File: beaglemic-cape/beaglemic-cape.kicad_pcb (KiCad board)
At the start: 2 copper layers, 79 parts, among them J1 USB_OTG, J10 MIC-04, J11 MIC-06, J12 MIC-08, J13 MIC-10, J14 MIC-12, J15 MIC-14, J16 MIC-01, J17 MIC-03, J18 MIC-05, J19 MIC-07, J2 PB_P1, J20 MIC-09, J21 MIC-11, J22 MIC-13, J23 MIC-15, J24 BBAI_FAN, J3 EXT_5V, J4 PB_P2, J5 BBAI_P8, J6 ICE40_EXT, J7 BBAI_P9, J8 MIC-00, J9 MIC-02, U1 74HC595, U2 74HC595, U3 AMS1117, U4 74HCT244, U5 SPM0423HD4H-WB, U6 SPM0423HD4H-WB

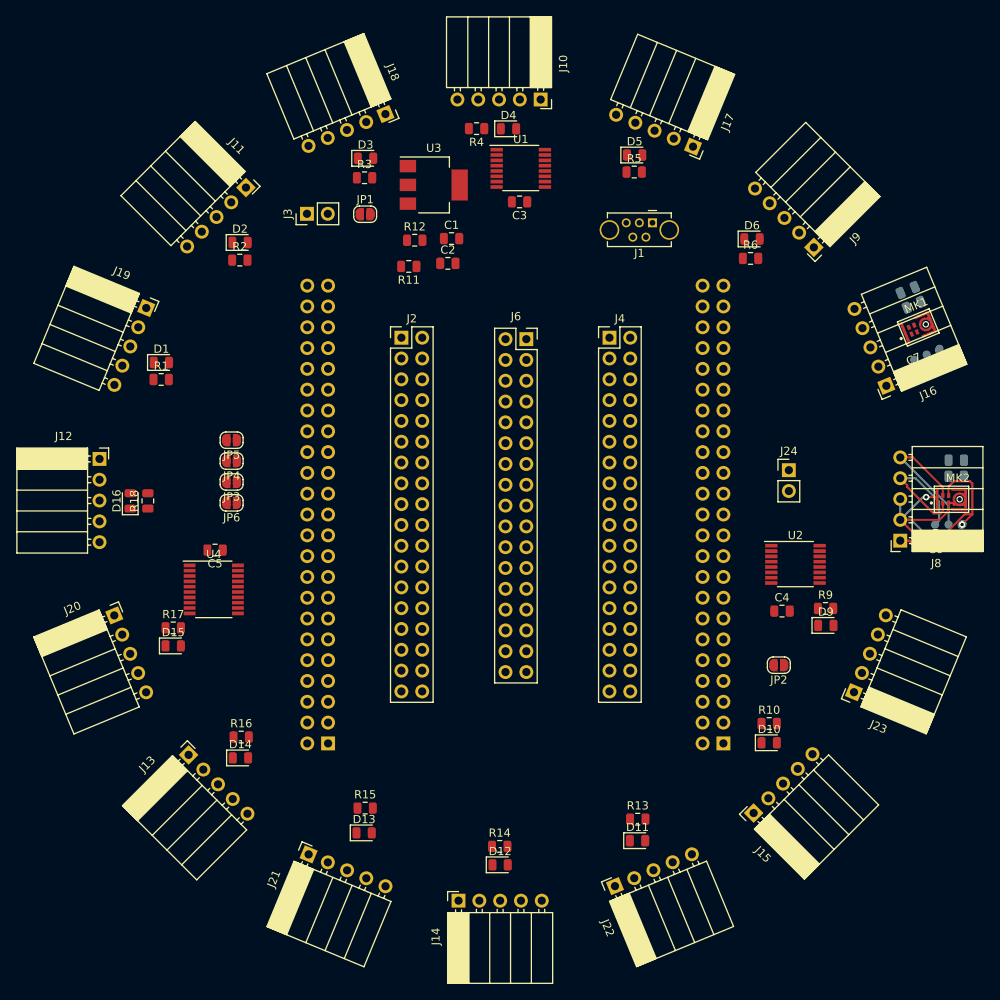
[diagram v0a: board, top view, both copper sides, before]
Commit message: beaglemic-cape: Shrink PCB to 100x100mm
Let's keep the PCB in the hobby price range.

Version 1.0-rc2

TODO: Route me!

Signed-off-by: Dimitar Dimitrov <dimitar@dinux.eu>
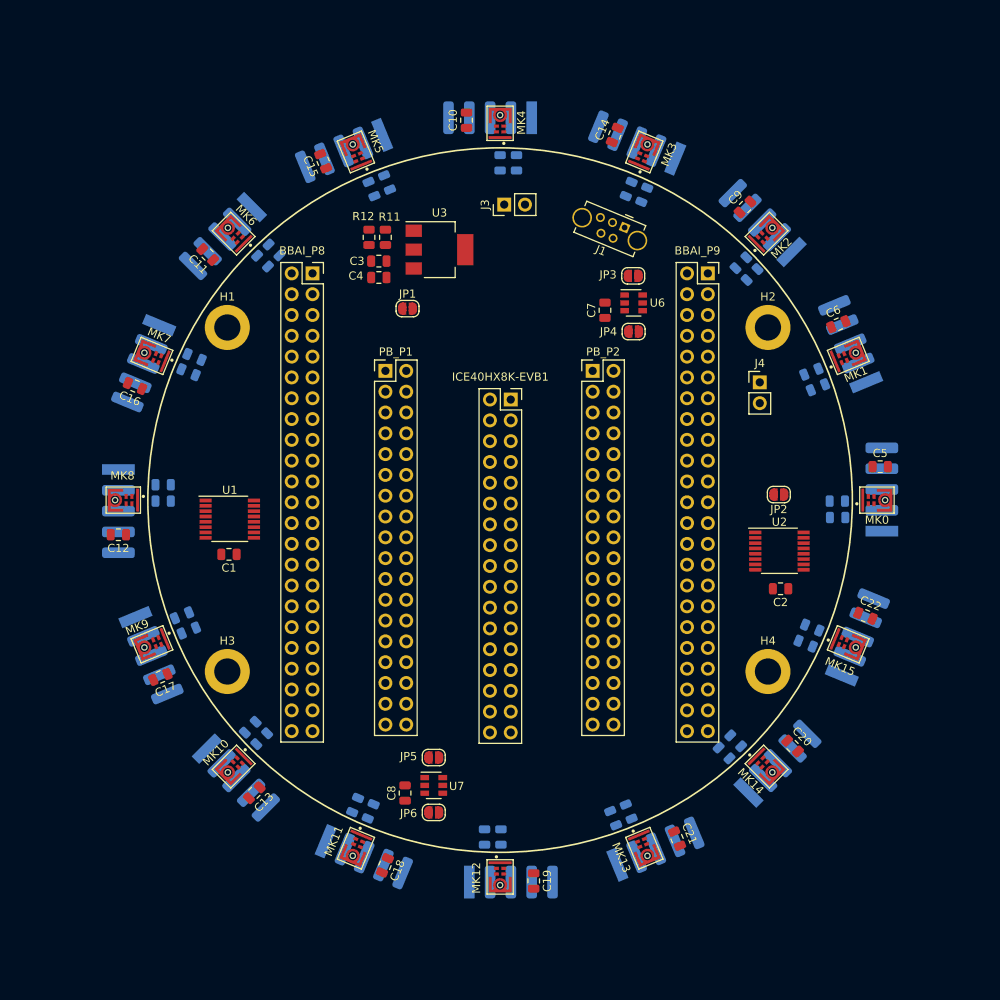
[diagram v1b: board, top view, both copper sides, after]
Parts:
- removed D16: LED-08, LED_SMD:LED_0805_2012Metric
- removed J10: MIC-04, Connector_PinSocket_2.54mm:PinSocket_1x05_P2.54mm_Horizontal
- removed J11: MIC-06, Connector_PinSocket_2.54mm:PinSocket_1x05_P2.54mm_Horizontal
- removed J12: MIC-08, Connector_PinSocket_2.54mm:PinSocket_1x05_P2.54mm_Horizontal
- removed J13: MIC-10, Connector_PinSocket_2.54mm:PinSocket_1x05_P2.54mm_Horizontal
- removed J14: MIC-12, Connector_PinSocket_2.54mm:PinSocket_1x05_P2.54mm_Horizontal
- removed J15: MIC-14, Connector_PinSocket_2.54mm:PinSocket_1x05_P2.54mm_Horizontal
- removed J16: MIC-01, Connector_PinSocket_2.54mm:PinSocket_1x05_P2.54mm_Horizontal
- removed J17: MIC-03, Connector_PinSocket_2.54mm:PinSocket_1x05_P2.54mm_Horizontal
- removed J18: MIC-05, Connector_PinSocket_2.54mm:PinSocket_1x05_P2.54mm_Horizontal
- removed J19: MIC-07, Connector_PinSocket_2.54mm:PinSocket_1x05_P2.54mm_Horizontal
- removed J2: PB_P1, Connector_PinHeader_2.54mm:PinHeader_2x18_P2.54mm_Vertical
- removed J20: MIC-09, Connector_PinSocket_2.54mm:PinSocket_1x05_P2.54mm_Horizontal
- removed J21: MIC-11, Connector_PinSocket_2.54mm:PinSocket_1x05_P2.54mm_Horizontal
- removed J22: MIC-13, Connector_PinSocket_2.54mm:PinSocket_1x05_P2.54mm_Horizontal
- removed J23: MIC-15, Connector_PinSocket_2.54mm:PinSocket_1x05_P2.54mm_Horizontal
- removed J24: BBAI_FAN, Connector_PinHeader_2.54mm:PinHeader_1x02_P2.54mm_Vertical
- removed J5: BBAI_P8, Connector_PinSocket_2.54mm:PinSocket_2x23_P2.54mm_Vertical
- removed J6: ICE40_EXT, Connector_PinSocket_2.54mm:PinSocket_2x17_P2.54mm_Vertical
- removed J7: BBAI_P9, Connector_PinSocket_2.54mm:PinSocket_2x23_P2.54mm_Vertical
- removed J8: MIC-00, Connector_PinSocket_2.54mm:PinSocket_1x05_P2.54mm_Horizontal
- removed J9: MIC-02, Connector_PinSocket_2.54mm:PinSocket_1x05_P2.54mm_Horizontal
- removed U4: 74HCT244, Package_SO:TSSOP-20_4.4x6.5mm_P0.65mm
- removed U5: SPM0423HD4H-WB, bga-6:BGA_6
- added BBAI_P8: BBAI_P8, Connector_PinSocket_2.54mm:PinSocket_2x23_P2.54mm_Vertical, F.Cu at (110.4, 66.4)
- added BBAI_P9: BBAI_P9, Connector_PinSocket_2.54mm:PinSocket_2x23_P2.54mm_Vertical, F.Cu at (158.7, 66.4)
- added C10: 100n, Capacitor_SMD:C_0805_2012Metric, F.Cu at (129.2, 47.7)
- added C11: 100n, Capacitor_SMD:C_0805_2012Metric, F.Cu at (97.6, 64.1)
- added C12: 100n, Capacitor_SMD:C_0805_2012Metric, F.Cu at (86.7, 98.3)
- added C13: 100n, Capacitor_SMD:C_0805_2012Metric, F.Cu at (103.3, 129.8)
- added C14: 100n, Capacitor_SMD:C_0805_2012Metric, F.Cu at (147.3, 49.5)
- added C15: 100n, Capacitor_SMD:C_0805_2012Metric, F.Cu at (111.7, 52.7)
- added C16: 100n, Capacitor_SMD:C_0805_2012Metric, F.Cu at (88.7, 80.1)
- added C17: 100n, Capacitor_SMD:C_0805_2012Metric, F.Cu at (91.8, 115.7)
- added C18: 100n, Capacitor_SMD:C_0805_2012Metric, F.Cu at (119.2, 138.7)
- added C19: 100n, Capacitor_SMD:C_0805_2012Metric, F.Cu at (137.4, 140.6)
- added C20: 100n, Capacitor_SMD:C_0805_2012Metric, F.Cu at (169.0, 124.1)
- added C21: 100n, Capacitor_SMD:C_0805_2012Metric, F.Cu at (154.9, 135.4)
- added C22: 100n, Capacitor_SMD:C_0805_2012Metric, F.Cu at (177.9, 108.2)
- added C8: 100n, Capacitor_SMD:C_0805_2012Metric, F.Cu at (121.7, 129.8)
- added C9: 100n, Capacitor_SMD:C_0805_2012Metric, F.Cu at (163.2, 58.3)
- added D0: LED-00, LED_SMD:LED_0805_2012Metric, B.Cu at (174.5, 94.2)
- added H1: MountingHole_Pad, MountingHole:MountingHole_3.2mm_M3_ISO14580_Pad, F.Cu at (100.0, 73.0)
- added H2: MountingHole_Pad, MountingHole:MountingHole_3.2mm_M3_ISO14580_Pad, F.Cu at (166.0, 73.0)
- added H3: MountingHole_Pad, MountingHole:MountingHole_3.2mm_M3_ISO14580_Pad, F.Cu at (100.0, 115.0)
- added H4: MountingHole_Pad, MountingHole:MountingHole_3.2mm_M3_ISO14580_Pad, F.Cu at (166.0, 115.0)
- added ICE40HX8K-EVB1: ICE40_EXT, Connector_PinSocket_2.54mm:PinSocket_2x17_P2.54mm_Vertical, F.Cu at (134.6, 81.8)
- added MK0: INMP621, inmp621-footprint:MK_INMP621, F.Cu at (179.3, 94.1)
- added MK10: INMP621, inmp621-footprint:MK_INMP621, F.Cu at (100.8, 126.6)
- added MK11: INMP621, inmp621-footprint:MK_INMP621, F.Cu at (115.7, 136.6)
- added MK12: INMP621, inmp621-footprint:MK_INMP621, F.Cu at (133.3, 140.1)
- added MK13: INMP621, inmp621-footprint:MK_INMP621, F.Cu at (150.9, 136.6)
- added MK14: INMP621, inmp621-footprint:MK_INMP621, F.Cu at (165.8, 126.6)
- added MK15: INMP621, inmp621-footprint:MK_INMP621, F.Cu at (175.8, 111.7)
- added MK3: INMP621, inmp621-footprint:MK_INMP621, F.Cu at (150.9, 51.6)
- added MK4: INMP621, inmp621-footprint:MK_INMP621, F.Cu at (133.3, 48.1)
- added MK5: INMP621, inmp621-footprint:MK_INMP621, F.Cu at (115.7, 51.6)
- added MK6: INMP621, inmp621-footprint:MK_INMP621, F.Cu at (100.8, 61.5)
- added MK7: INMP621, inmp621-footprint:MK_INMP621, F.Cu at (90.8, 76.5)
- added MK8: INMP621, inmp621-footprint:MK_INMP621, F.Cu at (87.3, 94.1)
- added MK9: INMP621, inmp621-footprint:MK_INMP621, F.Cu at (90.8, 111.7)
- added PB_P1: PB_P1, Connector_PinHeader_2.54mm:PinHeader_2x18_P2.54mm_Vertical, F.Cu at (119.3, 78.3)
- added PB_P2: PB_P2, Connector_PinHeader_2.54mm:PinHeader_2x18_P2.54mm_Vertical, F.Cu at (144.6, 78.3)
- added PHM-0: MIC-00, pinheader-smd:pinheader-5-smd-pads, B.Cu at (179.9, 87.7)
- added PHM-1: MIC-01, pinheader-smd:pinheader-5-smd-pads, B.Cu at (174.1, 70.3)
- added PHM-10: MIC-10, pinheader-smd:pinheader-5-smd-pads, B.Cu at (104.7, 131.6)
- added PHM-11: MIC-11, pinheader-smd:pinheader-5-smd-pads, B.Cu at (121.4, 139.6)
- added PHM-12: MIC-12, pinheader-smd:pinheader-5-smd-pads, B.Cu at (139.7, 140.7)
- added PHM-13: MIC-13, pinheader-smd:pinheader-5-smd-pads, B.Cu at (157.0, 134.7)
- added PHM-14: MIC-14, pinheader-smd:pinheader-5-smd-pads, B.Cu at (170.8, 122.6)
- added PHM-15: MIC-15, pinheader-smd:pinheader-5-smd-pads, B.Cu at (178.9, 106.1)
- added PHM-2: MIC-02, pinheader-smd:pinheader-5-smd-pads, B.Cu at (161.7, 56.6)
- added PHM-3: MIC-03, pinheader-smd:pinheader-5-smd-pads, B.Cu at (145.3, 48.5)
- added PHM-4: MIC-04, pinheader-smd:pinheader-5-smd-pads, B.Cu at (127.0, 47.4)
- added PHM-5: MIC-05, pinheader-smd:pinheader-5-smd-pads, B.Cu at (109.5, 53.4)
- added PHM-6: MIC-06, pinheader-smd:pinheader-5-smd-pads, B.Cu at (95.8, 65.5)
- added PHM-7: MIC-07, pinheader-smd:pinheader-5-smd-pads, B.Cu at (87.8, 82.1)
- added PHM-8: MIC-08, pinheader-smd:pinheader-5-smd-pads, B.Cu at (86.7, 100.5)
- added PHM-9: MIC-09, pinheader-smd:pinheader-5-smd-pads, B.Cu at (92.7, 117.7)
- added U7: 74AUC2G34, Package_TO_SOT_SMD:SOT-23-6, F.Cu at (125.2, 128.9)
- C2: value 10u -> 100n
- C4: value 100n -> 10u
- D1: value LED-07 -> LED-01; moved to B.Cu
- D10: value LED-14 -> LED-10; moved to B.Cu
- D11: value LED-13 -> LED-11; moved to B.Cu
- D12, D4, R1, R10, R13, R14, R15, R16, R17, R18, R2, R3, R4, R5, R6, R9: moved to B.Cu
- D13: value LED-11 -> LED-13; moved to B.Cu
- D14: value LED-10 -> LED-14; moved to B.Cu
- D15: value LED-09 -> LED-15; moved to B.Cu
- D2: value LED-06 -> LED-02; moved to B.Cu
- D3: value LED-05 -> LED-03; moved to B.Cu
- D5: value LED-03 -> LED-05; moved to B.Cu
- D6: value LED-02 -> LED-06; moved to B.Cu
- D7: value LED-01 -> LED-07
- D8: value LED-00 -> LED-08
- D9: value LED-15 -> LED-09; moved to B.Cu
- J4: value PB_P2 -> BBAI_FAN; footprint Connector_PinHeader_2.54mm:PinHeader_2x18_P2.54mm_Vertical -> Connector_PinHeader_2.54mm:PinHeader_1x02_P2.54mm_Vertical
- U6: value SPM0423HD4H-WB -> 74AUC2G34; footprint bga-6:BGA_6 -> Package_TO_SOT_SMD:SOT-23-6; moved to F.Cu
- moved D8 96.9 mm to (92.2, 94.2)
- moved D7 88.9 mm to (95.3, 78.5), turned to 337.5 degrees
- moved C5 81.8 mm to (179.7, 90.0), turned to 0 degrees
- moved D1 79.4 mm to (171.3, 78.4), turned to 202.5 degrees
- moved D15 78.0 mm to (171.4, 109.6), turned to 157.5 degrees
- moved D9 77.8 mm to (95.3, 110.0), turned to 22.5 degrees
- moved C4 63.9 mm to (118.5, 66.9), turned to 180 degrees
- moved D10 62.0 mm to (104.2, 123.2), turned to 45 degrees
- moved D2 61.2 mm to (162.7, 65.1), turned to 225 degrees
- moved D14 60.5 mm to (162.1, 123.5), turned to 135 degrees
- moved D6 59.8 mm to (104.3, 64.9), turned to 315 degrees
- moved C2 56.8 mm to (167.5, 104.9), turned to 180 degrees
- moved U1 55.6 mm to (100.3, 96.4)
- moved JP3 55.1 mm to (149.6, 66.7), turned to 0 degrees
- moved JP4 51.6 mm to (149.6, 73.5), turned to 0 degrees
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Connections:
- J4 pad 1: (no net) -> GND
- J4 pad 2: (no net) -> +5V
- MK2 pad 5: /MIC_D0 -> /MIC_D1
- R1 pad 1: Net-(D1-Pad1) -> Net-(D7-Pad1)
- R10 pad 1: Net-(D10-Pad1) -> Net-(D14-Pad1)
- R13 pad 1: Net-(D11-Pad1) -> Net-(D13-Pad1)
- R15 pad 1: Net-(D13-Pad1) -> Net-(D11-Pad1)
- R16 pad 1: Net-(D14-Pad1) -> Net-(D10-Pad1)
- R17 pad 1: Net-(D15-Pad1) -> Net-(D9-Pad1)
- R18 pad 1: Net-(D16-Pad1) -> Net-(D8-Pad1)
- R2 pad 1: Net-(D2-Pad1) -> Net-(D6-Pad1)
- R3 pad 1: Net-(D3-Pad1) -> Net-(D5-Pad1)
- R5 pad 1: Net-(D5-Pad1) -> Net-(D3-Pad1)
- R6 pad 1: Net-(D6-Pad1) -> Net-(D2-Pad1)
- R7 pad 1: Net-(D7-Pad1) -> Net-(D1-Pad1)
- R8 pad 1: Net-(D8-Pad1) -> Net-(D0-Pad1)
- R9 pad 1: Net-(D9-Pad1) -> Net-(D15-Pad1)
- U1 pad 1: Net-(D7-Pad2) -> Net-(D1-Pad2)
- U1 pad 15: Net-(D8-Pad2) -> Net-(D0-Pad2)
- U1 pad 2: Net-(D6-Pad2) -> Net-(D2-Pad2)
- U1 pad 3: Net-(D5-Pad2) -> Net-(D3-Pad2)
- U1 pad 5: Net-(D3-Pad2) -> Net-(D5-Pad2)
- U1 pad 6: Net-(D2-Pad2) -> Net-(D6-Pad2)
- U1 pad 7: Net-(D1-Pad2) -> Net-(D7-Pad2)
- U2 pad 1: Net-(D15-Pad2) -> Net-(D9-Pad2)
- U2 pad 15: Net-(D16-Pad2) -> Net-(D8-Pad2)
- U2 pad 2: Net-(D14-Pad2) -> Net-(D10-Pad2)
- U2 pad 3: Net-(D13-Pad2) -> Net-(D11-Pad2)
- U2 pad 5: Net-(D11-Pad2) -> Net-(D13-Pad2)
- U2 pad 6: Net-(D10-Pad2) -> Net-(D14-Pad2)
- U2 pad 7: Net-(D9-Pad2) -> Net-(D15-Pad2)
- U6 pad 1: GND -> /MIC_CLK
- U6 pad 2: +3V3 -> GND
- U6 pad 3: GND -> /MIC_CLK
- U6 pad 4: /Microphone Headers/CLK0 -> /Microphone Headers/CLK1
- U6 pad 5: /MIC_D0 -> +3V3
- U6 pad 6: +3V3 -> /Microphone Headers/CLK0
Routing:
- net GND: track 31.2 -> 0.00 mm, vias 1 -> 0
- net +3V3: track 20.4 -> 0.00 mm, vias 1 -> 0
- net /MIC_D0: track 18.4 -> 0.00 mm
- net /Microphone Headers/CLK0: track 17.2 -> 0.00 mm
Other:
- net class Power added: clearance 0.2, trace_width 0.4, via_dia 0.8, via_drill 0.4

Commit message: beaglemic-cape: Route PCB
WARNING - NOT TESTED YET!

Signed-off-by: Dimitar Dimitrov <dimitar@dinux.eu>
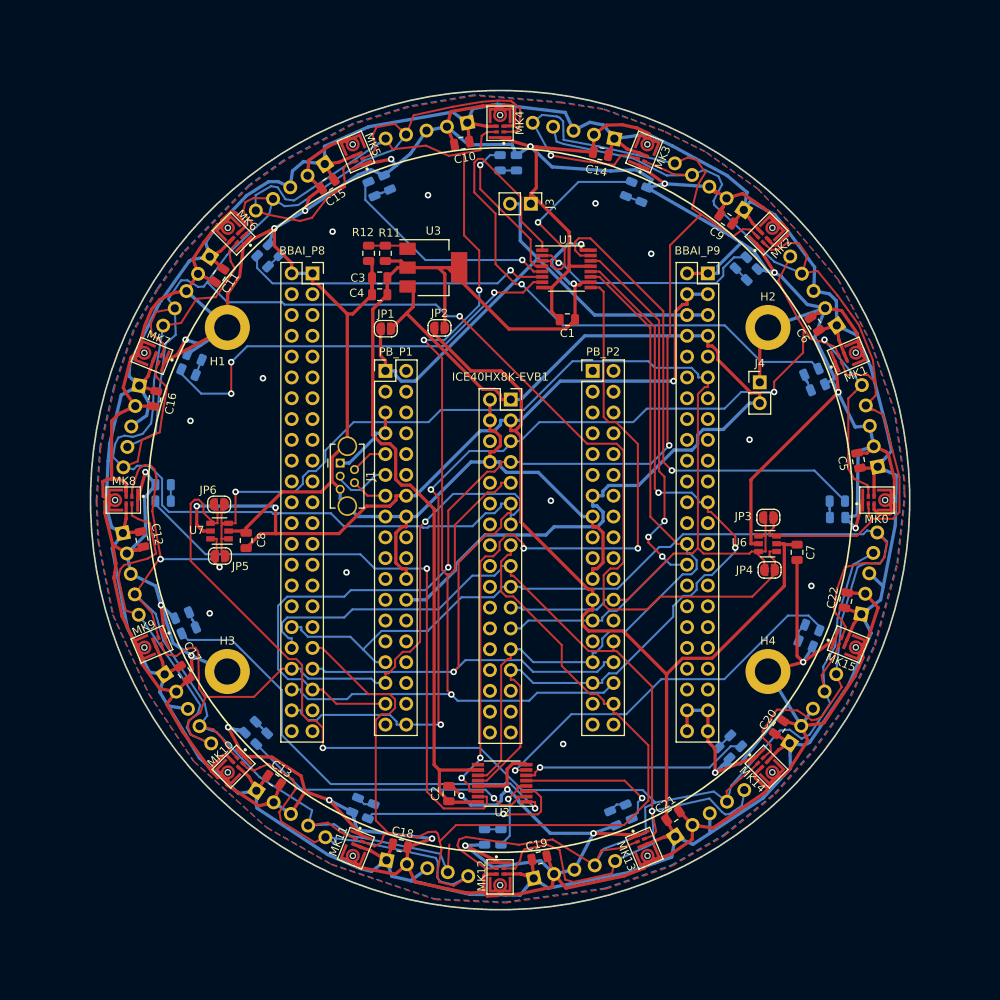
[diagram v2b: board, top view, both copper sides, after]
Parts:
- PHM-0, PHM-1, PHM-10, PHM-11, PHM-12, PHM-13, PHM-14, PHM-15, PHM-2, PHM-3, PHM-4, PHM-5, PHM-6, PHM-7, PHM-8, PHM-9: footprint pinheader-smd:pinheader-5-smd-pads -> Connector_PinSocket_2.54mm:PinSocket_1x05_P2.54mm_Vertical
- moved U1 51.2 mm to (141.4, 65.8)
- moved C1 50.3 mm to (141.5, 72.0)
- moved C2 47.6 mm to (127.0, 129.9), turned to 90 degrees
- moved JP2 46.2 mm to (125.9, 73.0), turned to 0 degrees
- moved JP6 45.8 mm to (99.0, 94.6), turned to 180 degrees
- moved J1 45.1 mm to (113.8, 89.5), turned to 270 degrees
- moved U2 44.2 mm to (133.6, 128.7), turned to 180 degrees
- moved U7 40.6 mm to (99.0, 97.8), turned to 180 degrees
- moved C7 37.7 mm to (169.6, 100.5), turned to 270 degrees
- moved C8 36.4 mm to (102.3, 99.0)
- moved JP5 35.9 mm to (99.1, 100.9), turned to 180 degrees
- moved JP3 33.8 mm to (166.1, 96.2)
- moved U6 33.6 mm to (165.9, 99.4)
- moved JP4 33.5 mm to (166.2, 102.6)
- moved JP1 3.61 mm to (119.3, 73.2)
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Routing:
- net GND: track 0.00 -> 955.6 mm, vias 0 -> 33
- net +3V3: track 0.00 -> 649.4 mm, vias 0 -> 3
- net /Microphone Headers/CLK1: track 0.00 -> 215.1 mm, vias 0 -> 1
- net /Microphone Headers/CLK3: track 0.00 -> 196.5 mm, vias 0 -> 1
- net /MIC_D2: track 0.00 -> 188.6 mm, vias 0 -> 3
- net /MIC_D3: track 0.00 -> 170.3 mm, vias 0 -> 1
- net /MIC_D1: track 0.00 -> 169.2 mm, vias 0 -> 3
- net /MIC_D5: track 0.00 -> 163.2 mm
- net /MIC_D0: track 0.00 -> 145.1 mm, vias 0 -> 4
- net /MIC_CLK: track 0.00 -> 144.1 mm, vias 0 -> 1
- net /MIC_D7: track 0.00 -> 141.9 mm
- net +3.3VP: track 0.00 -> 135.7 mm, vias 0 -> 2
- net /MIC_D4: track 0.00 -> 124.9 mm, vias 0 -> 1
- net /MIC_D6: track 0.00 -> 122.5 mm, vias 0 -> 1
- net +5V: track 0.00 -> 121.8 mm
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- added copper zone on B.Cu, net GND
- added copper zone on F.Cu, net GND
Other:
- board outline added: 100 x 100 mm
- board text added: "CC BY-SA 4.0"
- board text added: "beaglemic-cape v1.0 dimitar@dinux.eu"
